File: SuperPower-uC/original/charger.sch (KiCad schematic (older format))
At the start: 24 parts, among them J2 DNP/JST_ZH_S2B_thru, J3 DNP/JST_XH_S2B_thru, Q2 DMN3018SSD, Q3 2N7002A, Q4 DMP3028LSD, U2 LTC4162EUFD-LAD

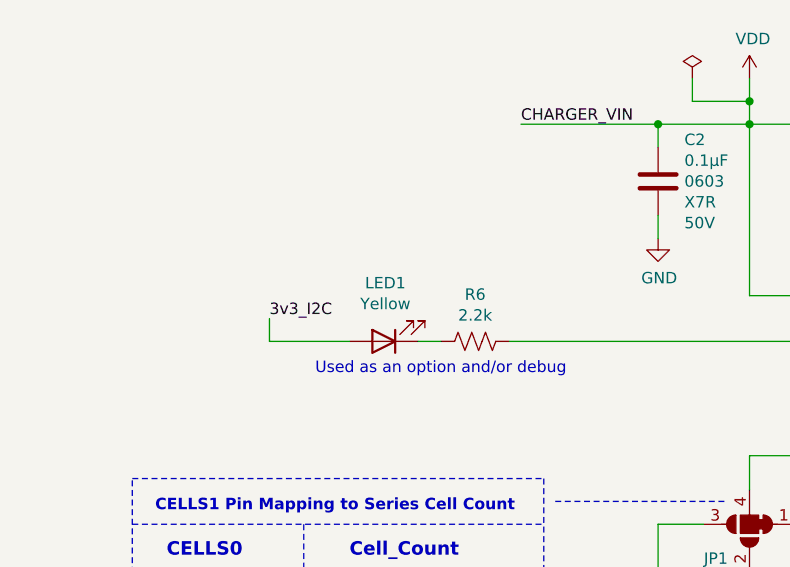
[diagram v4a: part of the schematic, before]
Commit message: Update LED symbols
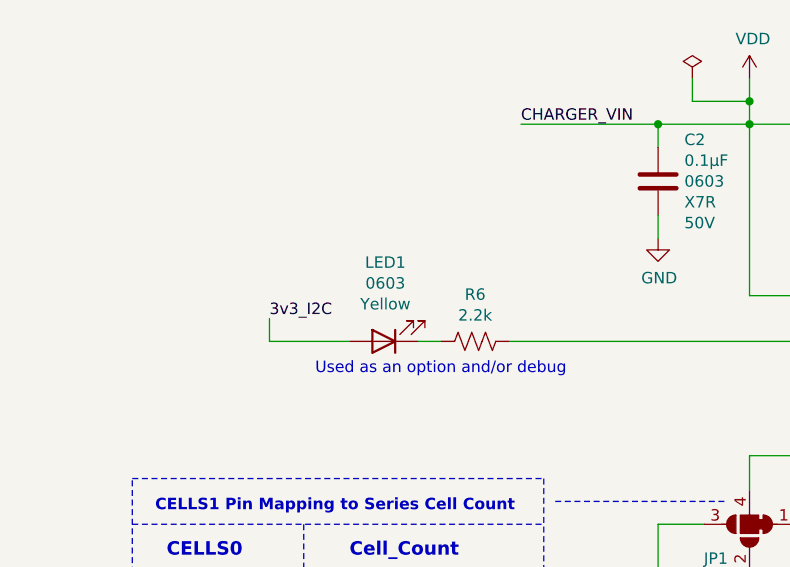
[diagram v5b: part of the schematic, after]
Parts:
- LED1: Farnell_check_date 2020-11-23 -> 2020-12-07; Farnell_link https://uk.farnell.com/wurth-elektronik/150060ys75000/led-0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 -> https://fr.farnell.com/wurth-elektronik/150060ys75000/led-0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; Farnell_price_qt=1 (none) -> -; Farnell_price_qt=10 (none) -> 0.139€; Farnell_price_qt=100 (none) -> 0.115€; Farnell_price_qt=1000 (none) -> 0.0979€; Farnell_price_qt=5 £0.144 -> (none); Farnell_stock 16778 -> 15,254; LCSC_check_date (none) -> 2020-12-07; LCSC_price_qt=1 (none) -> -; LCSC_price_qt=10 (none) -> -; LCSC_price_qt=100 (none) -> -; LCSC_price_qt=1000 (none) -> -; LCSC_stock (none) -> -; Mouser_check_date 2020-11-23 -> 2020-12-07; Mouser_price_qt=10 (none) -> $0.151; Mouser_price_qt=100 (none) -> $0.115; Mouser_price_qt=1000 (none) -> $0.107; Mouser_stock 57491 -> 44,294; RS_check_date 2020-11-23 -> 2020-12-07; RS_price_qt=1 (none) -> -; RS_price_qt=10 (none) -> -; RS_price_qt=1000 (none) -> 0.074€; RS_stock 1100 -> 400
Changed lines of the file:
@@
 Text Label 1650 3650 0    50   ~ 0
 3v3_I2C
-$Comp
-L 150060ys75000:150060YS75000_0603 LED1
-U 1 1 5FC58854
-P 2150 3750
-F 0 "LED1" H 2143 3495 50  0000 C CNN
-F 1 "150060YS75000_0603" H 2143 3586 50  0001 C CNN
-F 2 "LED_SMD:LED_0603_1608Metric" H 2150 3750 50  0001 C CNN
-F 3 "~" H 2150 3750 50  0001 C CNN
-F 4 "Wurth Elektronik " H 2150 3750 50  0001 C CNN "Mfr_name"
-F 5 "150060YS75000" H 2150 3750 50  0001 C CNN "Mfr_no"
-F 6 "0603" H 2350 3850 50  0001 C CNN "Package"
-F 7 "Yellow" H 2143 3586 50  0000 C CNN "Color"
-F 8 "https://octopart.com/search?autosugg_idx=0&currency=USD&oq=150060YS75000&q=150060YS75000&specs=1" H 2150 3750 50  0001 C CNN "Octopart_link"
-F 9 "https://eu.mouser.com/ProductDetail/Wurth-Elektronik/150060YS75000?qs=LlUlMxKIyB0nKmwefHgtZw%3D%3D" H 2150 3750 50  0001 C CNN "Mouser_link"
-F 10 "710-150060YS75000 " H 2150 3750 50  0001 C CNN "Mouser_ref"
-F 11 "2020-11-23" H 2150 3750 50  0001 C CNN "Mouser_check_date"
-F 12 "$0.151" H 2300 3550 50  0001 C CNN "Mouser_price_qt=1"
-F 13 "57491" H 2150 3750 50  0001 C CNN "Mouser_stock"
-F 14 "https://uk.farnell.com/wurth-elektronik/150060ys75000/led-0603-yellow-120mcd-590nm/dp/2322074?st=150060YS75000" H 2150 3750 50  0001 C CNN "Farnell_link"
-F 15 "2322074" H 2150 3750 50  0001 C CNN "Farnell_ref"
-F 16 "2020-11-23" H 2150 3750 50  0001 C CNN "Farnell_check_date"
-F 17 "£0.144" H 2150 3750 50  0001 C CNN "Farnell_price_qt=5"
-F 18 "16778" H 2150 3750 50  0001 C CNN "Farnell_stock"
-F 19 "-" H 2150 3750 50  0001 C CNN "LCSC_link"
-F 20 "-" H 2150 3750 50  0001 C CNN "LCSC_ref"
-F 21 "https://fr.rs-online.com/web/p/led/8154219/" H 2150 3750 50  0001 C CNN "RS_link"
-F 22 "815-4219" H 2150 3750 50  0001 C CNN "RS_ref"
-F 23 "2020-11-23" H 2150 3750 50  0001 C CNN "RS_check_date"
-F 24 "0.101€" H 2150 3750 50  0001 C CNN "RS_price_qt=100"
-F 25 "1100" H 2150 3750 50  0001 C CNN "RS_stock"
-F 26 "TO_CHECK" H 2150 3750 50  0001 C CNN "Status"
-F 27 "1.00" H 2150 3750 50  0001 C CNN "Release_version"
-F 28 "2020-11-23" H 2150 3750 50  0001 C CNN "Release_date"
-F 29 "ManWithNoName" H 2150 3750 50  0001 C CNN "Designer"
-	1    2150 3750
-	-1   0    0    1
-$EndComp
 Text Notes 3450 1800 0    79   Italic 0
 Iin(max) = 32mV/Rsnsi\nIchg(max) = 32mV/Rsnsb
@@
 	1    0    0    -1
 $EndComp
+$Comp
+L 150060ys75000:150060YS75000_0603 LED1
+U 1 1 5FCED4FE
+P 2150 3750
+F 0 "LED1" H 2143 3405 50  0000 C CNN
+F 1 "150060YS75000_0603" H 2150 3650 50  0001 C CNN
+F 2 "LED_SMD:LED_0603_1608Metric" H 2150 3750 50  0001 C CNN
+F 3 "https://www.we-online.com/catalog/datasheet/150060YS75000.pdf" H 2150 3750 50  0001 C CNN
+F 4 "Wurth Elektronik " H 2150 3750 50  0001 C CNN "Mfr_name"
+F 5 "150060YS75000" H 2150 3750 50  0001 C CNN "Mfr_no"
+F 6 "0603" H 2143 3496 50  0000 C CNN "Package"
+F 7 "Yellow" H 2143 3587 50  0000 C CNN "Color"
+F 8 "https://octopart.com/search?autosugg_idx=0&currency=USD&oq=150060YS75000&q=150060YS75000&specs=1" H 2150 3750 50  0001 C CNN "Octopart_link"
+F 9 "https://fr.farnell.com/wurth-elektronik/150060ys75000/led-0603-jaune-120mcd-590nm/dp/2322074?st=150060ys75000" H 2150 3750 50  0001 C CNN "Farnell_link"
+F 10 "2322074" H 2150 3750 50  0001 C CNN "Farnell_ref"
+F 11 "2020-12-07" H 2150 3750 50  0001 C CNN "Farnell_check_date"
+F 12 "-" H 2150 3750 50  0001 C CNN "Farnell_price_qt=1"
+F 13 "0.139€" H 2150 3750 50  0001 C CNN "Farnell_price_qt=10"
+F 14 "0.115€" H 2150 3750 50  0001 C CNN "Farnell_price_qt=100"
+F 15 "0.0979€" H 2150 3750 50  0001 C CNN "Farnell_price_qt=1000"
+F 16 "15,254" H 2150 3750 50  0001 C CNN "Farnell_stock"
+F 17 "-" H 2150 3750 50  0001 C CNN "LCSC_link"
+F 18 "-" H 2150 3750 50  0001 C CNN "LCSC_ref"
+F 19 "2020-12-07" H 2150 3750 50  0001 C CNN "LCSC_check_date"
+F 20 "-" H 2150 3750 50  0001 C CNN "LCSC_price_qt=1"
+F 21 "-" H 2150 3750 50  0001 C CNN "LCSC_price_qt=10"
+F 22 "-" H 2150 3750 50  0001 C CNN "LCSC_price_qt=100"
+F 23 "-" H 2150 3750 50  0001 C CNN "LCSC_price_qt=1000"
+F 24 "-" H 2150 3750 50  0001 C CNN "LCSC_stock"
+F 25 "https://eu.mouser.com/ProductDetail/Wurth-Elektronik/150060YS75000?qs=LlUlMxKIyB0nKmwefHgtZw%3D%3D" H 2150 3750 50  0001 C CNN "Mouser_link"
+F 26 "710-150060YS75000 " H 2150 3750 50  0001 C CNN "Mouser_ref"
+F 27 "2020-12-07" H 2150 3750 50  0001 C CNN "Mouser_check_date"
+F 28 "$0.151" H 2300 3550 50  0001 C CNN "Mouser_price_qt=1"
+F 29 "$0.151" H 2300 3550 50  0001 C CNN "Mouser_price_qt=10"
+F 30 "$0.115" H 2300 3550 50  0001 C CNN "Mouser_price_qt=100"
+F 31 "$0.107" H 2300 3550 50  0001 C CNN "Mouser_price_qt=1000"
+F 32 "44,294" H 2150 3750 50  0001 C CNN "Mouser_stock"
+F 33 "https://fr.rs-online.com/web/p/led/8154219/" H 2150 3750 50  0001 C CNN "RS_link"
+F 34 "815-4219" H 2150 3750 50  0001 C CNN "RS_ref"
+F 35 "2020-12-07" H 2150 3750 50  0001 C CNN "RS_check_date"
+F 36 "-" H 2150 3750 50  0001 C CNN "RS_price_qt=1"
+F 37 "-" H 2150 3750 50  0001 C CNN "RS_price_qt=10"
+F 38 "0.101€" H 2150 3750 50  0001 C CNN "RS_price_qt=100"
+F 39 "0.074€" H 2150 3750 50  0001 C CNN "RS_price_qt=1000"
+F 40 "400" H 2150 3750 50  0001 C CNN "RS_stock"
+F 41 "TO_CHECK" H 2150 3750 50  0001 C CNN "Status"
+F 42 "1.00" H 2150 3750 50  0001 C CNN "Release_version"
+F 43 "2020-11-23" H 2150 3750 50  0001 C CNN "Release_date"
+F 44 "ManWithNoName" H 2150 3750 50  0001 C CNN "Designer"
+	1    2150 3750
+	-1   0    0    1
+$EndComp
 $EndSCHEMATC

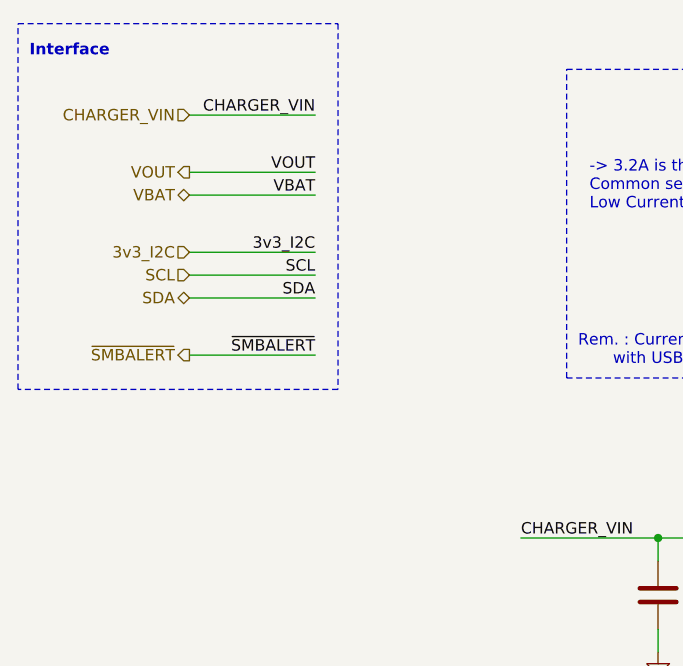
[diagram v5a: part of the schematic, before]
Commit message: Add test points to the interface
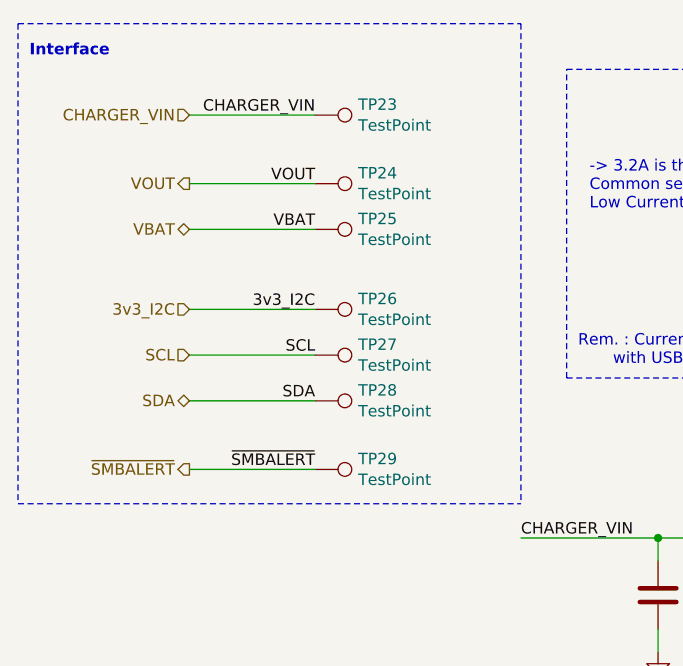
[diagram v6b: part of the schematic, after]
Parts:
- added TP23, TP24, TP25, TP26, TP27, TP28, TP29: TestPoint, TestPoint:TestPoint_Pad_D1.0mm, symbol Connector:TestPoint
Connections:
- net 3v3_I2C: now also TP26.1
- net SCL: now also TP27.1
- net SDA: now also TP28.1
- net VBAT: now also TP25.1
- net VDD: now also TP23.1
- net VOUT: now also TP24.1
- net ~SMBALERT: now also TP29.1
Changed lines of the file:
@@
 Comment4 ""
 $EndDescr
-Text HLabel 1300 1200 0    50   Output ~ 0
+Text HLabel 1300 1250 0    50   Output ~ 0
 VOUT
-Text HLabel 1300 1300 0    50   BiDi ~ 0
+Text HLabel 1300 1450 0    50   BiDi ~ 0
 VBAT
 $Comp
@@
 	4600 3950 5000 3950
 Wire Wire Line
-	1850 1300 1300 1300
+	1850 1450 1300 1450
 $Comp
 L power:GND #PWR021
@@
 	7500 850  7500 1450
 Wire Wire Line
-	1850 1200 1300 1200
+	1850 1250 1300 1250
 Wire Notes Line
 	6400 1000 7900 1000
@@
 Text Notes 1400 5450 0    50   ~ 0
 See Table 5 in the datasheet
-Text HLabel 1300 1550 0    50   Input ~ 0
+Text HLabel 1300 1800 0    50   Input ~ 0
 3v3_I2C
 Wire Wire Line
-	1300 1550 1850 1550
-Text Label 1850 1550 2    50   ~ 0
+	1300 1800 1850 1800
+Text Label 1850 1800 2    50   ~ 0
 3v3_I2C
 Text Label 4600 3850 0    50   ~ 0
@@
 	7850 1450 7500 1450
 Connection ~ 7500 1450
-Text Label 1850 1200 2    50   ~ 0
+Text Label 1850 1250 2    50   ~ 0
 VOUT
 Text Label 8150 4350 2    50   ~ 0
 VBAT
-Text HLabel 1300 1650 0    50   Input ~ 0
+Text HLabel 1300 2000 0    50   Input ~ 0
 SCL
-Text HLabel 1300 1750 0    50   BiDi ~ 0
+Text HLabel 1300 2200 0    50   BiDi ~ 0
 SDA
 Wire Wire Line
-	1300 1750 1850 1750
-Wire Wire Line
-	1300 1650 1850 1650
-Text Label 1850 1300 2    50   ~ 0
+	1300 2200 1850 2200
+Wire Wire Line
+	1300 2000 1850 2000
+Text Label 1850 1450 2    50   ~ 0
 VBAT
-Text Label 1850 1650 2    50   ~ 0
+Text Label 1850 2000 2    50   ~ 0
 SCL
-Text Label 1850 1750 2    50   ~ 0
+Text Label 1850 2200 2    50   ~ 0
 SDA
 Text Label 4600 3950 0    50   ~ 0
@@
 Text Label 4600 3750 0    50   ~ 0
 ~SMBALERT
-Text HLabel 1300 2000 0    50   Output ~ 0
+Text HLabel 1300 2500 0    50   Output ~ 0
 ~SMBALERT
 Wire Wire Line
-	1850 2000 1300 2000
-Text Label 1850 2000 2    50   ~ 0
+	1850 2500 1300 2500
+Text Label 1850 2500 2    50   ~ 0
 ~SMBALERT
 $Comp
@@
 Text Notes 600  700  0    50   ~ 10
 Interface
-Wire Notes Line
-	550  550  1950 550
-Wire Notes Line
-	1950 550  1950 2150
-Wire Notes Line
-	1950 2150 550  2150
-Wire Notes Line
-	550  2150 550  550
 $Comp
 L cl31b106kahnnne:CL31B106KAHNNNE C7
@@
 	-1   0    0    1
 $EndComp
+Wire Notes Line
+	550  2650 2750 2650
+Wire Notes Line
+	550  550  2750 550
+$Comp
+L Connector:TestPoint TP23
+U 1 1 5FD90BDE
+P 1850 950
+F 0 "TP23" V 1804 1138 50  0000 L CNN
+F 1 "TestPoint" V 1895 1138 50  0000 L CNN
+F 2 "TestPoint:TestPoint_Pad_D1.0mm" H 2050 950 50  0001 C CNN
+F 3 "~" H 2050 950 50  0001 C CNN
+	1    1850 950
+	0    1    1    0
+$EndComp
+$Comp
+L Connector:TestPoint TP24
+U 1 1 5FD91067
+P 1850 1250
+F 0 "TP24" V 1804 1438 50  0000 L CNN
+F 1 "TestPoint" V 1895 1438 50  0000 L CNN
+F 2 "TestPoint:TestPoint_Pad_D1.0mm" H 2050 1250 50  0001 C CNN
+F 3 "~" H 2050 1250 50  0001 C CNN
+	1    1850 1250
+	0    1    1    0
+$EndComp
+$Comp
+L Connector:TestPoint TP25
+U 1 1 5FD9140F
+P 1850 1450
+F 0 "TP25" V 1804 1638 50  0000 L CNN
+F 1 "TestPoint" V 1895 1638 50  0000 L CNN
+F 2 "TestPoint:TestPoint_Pad_D1.0mm" H 2050 1450 50  0001 C CNN
+F 3 "~" H 2050 1450 50  0001 C CNN
+	1    1850 1450
+	0    1    1    0
+$EndComp
+$Comp
+L Connector:TestPoint TP26
+U 1 1 5FD9160B
+P 1850 1800
+F 0 "TP26" V 1804 1988 50  0000 L CNN
+F 1 "TestPoint" V 1895 1988 50  0000 L CNN
+F 2 "TestPoint:TestPoint_Pad_D1.0mm" H 2050 1800 50  0001 C CNN
+F 3 "~" H 2050 1800 50  0001 C CNN
+	1    1850 1800
+	0    1    1    0
+$EndComp
+$Comp
+L Connector:TestPoint TP27
+U 1 1 5FD91A28
+P 1850 2000
+F 0 "TP27" V 1804 2188 50  0000 L CNN
+F 1 "TestPoint" V 1895 2188 50  0000 L CNN
+F 2 "TestPoint:TestPoint_Pad_D1.0mm" H 2050 2000 50  0001 C CNN
+F 3 "~" H 2050 2000 50  0001 C CNN
+	1    1850 2000
+	0    1    1    0
+$EndComp
+$Comp
+L Connector:TestPoint TP28
+U 1 1 5FD91C9F
+P 1850 2200
+F 0 "TP28" V 1804 2388 50  0000 L CNN
+F 1 "TestPoint" V 1895 2388 50  0000 L CNN
+F 2 "TestPoint:TestPoint_Pad_D1.0mm" H 2050 2200 50  0001 C CNN
+F 3 "~" H 2050 2200 50  0001 C CNN
+	1    1850 2200
+	0    1    1    0
+$EndComp
+$Comp
+L Connector:TestPoint TP29
+U 1 1 5FD91E2F
+P 1850 2500
+F 0 "TP29" V 1804 2688 50  0000 L CNN
+F 1 "TestPoint" V 1895 2688 50  0000 L CNN
+F 2 "TestPoint:TestPoint_Pad_D1.0mm" H 2050 2500 50  0001 C CNN
+F 3 "~" H 2050 2500 50  0001 C CNN
+	1    1850 2500
+	0    1    1    0
+$EndComp
+Wire Notes Line
+	2750 550  2750 2650
+Wire Notes Line
+	550  550  550  2650
 $EndSCHEMATC

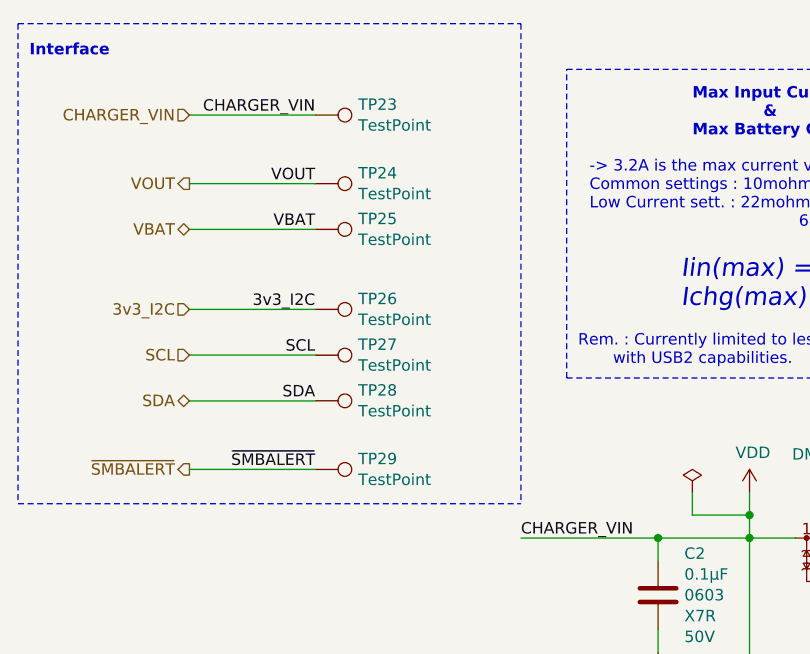
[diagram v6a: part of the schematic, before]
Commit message: Started layout and placed components related to its function and interface (first draft)
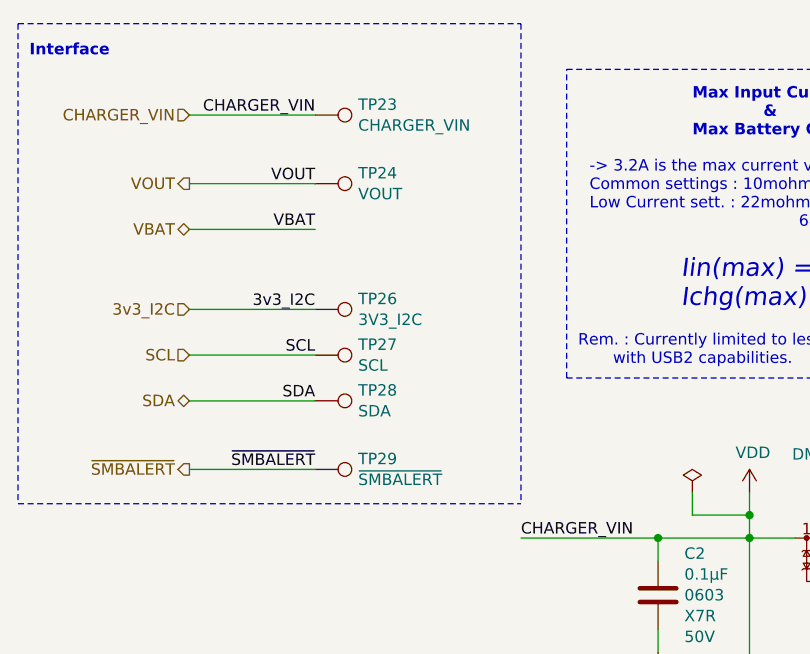
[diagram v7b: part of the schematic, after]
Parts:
- removed TP25: TestPoint, TestPoint:TestPoint_Pad_D1.0mm, symbol Connector:TestPoint
- TP23: value TestPoint -> CHARGER_VIN
- TP24: value TestPoint -> VOUT
- TP26: value TestPoint -> 3V3_I2C
- TP27: value TestPoint -> SCL
- TP28: value TestPoint -> SDA
- TP29: value TestPoint -> ~SMBALERT
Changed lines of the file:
@@
 P 1850 950
 F 0 "TP23" V 1804 1138 50  0000 L CNN
-F 1 "TestPoint" V 1895 1138 50  0000 L CNN
+F 1 "CHARGER_VIN" V 1895 1138 50  0000 L CNN
 F 2 "TestPoint:TestPoint_Pad_D1.0mm" H 2050 950 50  0001 C CNN
 F 3 "~" H 2050 950 50  0001 C CNN
@@
 P 1850 1250
 F 0 "TP24" V 1804 1438 50  0000 L CNN
-F 1 "TestPoint" V 1895 1438 50  0000 L CNN
+F 1 "VOUT" V 1895 1438 50  0000 L CNN
 F 2 "TestPoint:TestPoint_Pad_D1.0mm" H 2050 1250 50  0001 C CNN
 F 3 "~" H 2050 1250 50  0001 C CNN
 	1    1850 1250
-	0    1    1    0
-$EndComp
-$Comp
-L Connector:TestPoint TP25
-U 1 1 5FD9140F
-P 1850 1450
-F 0 "TP25" V 1804 1638 50  0000 L CNN
-F 1 "TestPoint" V 1895 1638 50  0000 L CNN
-F 2 "TestPoint:TestPoint_Pad_D1.0mm" H 2050 1450 50  0001 C CNN
-F 3 "~" H 2050 1450 50  0001 C CNN
-	1    1850 1450
 	0    1    1    0
 $EndComp
@@
 P 1850 1800
 F 0 "TP26" V 1804 1988 50  0000 L CNN
-F 1 "TestPoint" V 1895 1988 50  0000 L CNN
+F 1 "3V3_I2C" V 1895 1988 50  0000 L CNN
 F 2 "TestPoint:TestPoint_Pad_D1.0mm" H 2050 1800 50  0001 C CNN
 F 3 "~" H 2050 1800 50  0001 C CNN
@@
 P 1850 2000
 F 0 "TP27" V 1804 2188 50  0000 L CNN
-F 1 "TestPoint" V 1895 2188 50  0000 L CNN
+F 1 "SCL" V 1895 2188 50  0000 L CNN
 F 2 "TestPoint:TestPoint_Pad_D1.0mm" H 2050 2000 50  0001 C CNN
 F 3 "~" H 2050 2000 50  0001 C CNN
@@
 P 1850 2200
 F 0 "TP28" V 1804 2388 50  0000 L CNN
-F 1 "TestPoint" V 1895 2388 50  0000 L CNN
+F 1 "SDA" V 1895 2388 50  0000 L CNN
 F 2 "TestPoint:TestPoint_Pad_D1.0mm" H 2050 2200 50  0001 C CNN
 F 3 "~" H 2050 2200 50  0001 C CNN
@@
 P 1850 2500
 F 0 "TP29" V 1804 2688 50  0000 L CNN
-F 1 "TestPoint" V 1895 2688 50  0000 L CNN
+F 1 "~SMBALERT" V 1895 2688 50  0000 L CNN
 F 2 "TestPoint:TestPoint_Pad_D1.0mm" H 2050 2500 50  0001 C CNN
 F 3 "~" H 2050 2500 50  0001 C CNN
